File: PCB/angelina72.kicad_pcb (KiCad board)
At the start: 2 copper layers, 176.4 x 111.6 mm, 88 parts, among them J1 MJ-4PP-9, J2 LED, SW1 KEY_SWITCH, SW10 KEY_SWITCH, SW11 KEY_SWITCH, SW12 KEY_SWITCH, SW13 KEY_SWITCH, SW14 KEY_SWITCH, SW15 KEY_SWITCH, SW16 KEY_SWITCH, SW17 KEY_SWITCH, SW18 KEY_SWITCH, SW19 KEY_SWITCH, SW2 KEY_SWITCH, SW20 KEY_SWITCH, SW21 KEY_SWITCH, SW22 KEY_SWITCH, SW23 KEY_SWITCH, SW24 KEY_SWITCH, SW25 KEY_SWITCH, SW26 KEY_SWITCH, SW27 KEY_SWITCH, SW28 KEY_SWITCH, SW29 KEY_SWITCH, SW3 KEY_SWITCH, SW30 KEY_SWITCH, SW31 KEY_SWITCH, SW32 KEY_SWITCH, SW33 KEY_SWITCH, SW34 KEY_SWITCH, SW35 KEY_SWITCH, SW36 KEY_SWITCH, SW4 KEY_SWITCH, SW5 KEY_SWITCH, SW6 KEY_SWITCH, SW7 KEY_SWITCH, SW8 KEY_SWITCH, SW9 KEY_SWITCH, U1 ProMicro

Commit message: Update PCB, top plate
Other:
- outline, holes or cut-outs redrawn
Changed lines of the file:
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@@
   (gr_arc (start 65.649991 79.032478) (end 66.119003 78.949782) (angle -180) (layer Edge.Cuts) (width 0.05))
   (gr_arc (start 65.319197 77.156422) (end 64.850181 77.239123) (angle -180) (layer Edge.Cuts) (width 0.05))
-  (gr_line (start 74.6796 119.271451) (end 68.582435 120.346568) (layer Edge.Cuts) (width 0.05))
-  (gr_arc (start 68.665108 120.815566) (end 68.582435 120.346568) (angle -180.0026468) (layer Edge.Cuts) (width 0.05))
-  (gr_arc (start 66.789075 121.146382) (end 66.87175 121.615378) (angle -180.0026468) (layer Edge.Cuts) (width 0.05))
+  (gr_line (start 74.6796 119.271451) (end 68.934197 120.284543) (layer Edge.Cuts) (width 0.05))
+  (gr_arc (start 69.016871 120.753541) (end 68.934197 120.284543) (angle -180.0026468) (layer Edge.Cuts) (width 0.05))
+  (gr_arc (start 67.140837 121.084357) (end 67.223513 121.553353) (angle -180.0026468) (layer Edge.Cuts) (width 0.05))
   (gr_arc (start 188.469026 37.71159) (end 188.945278 37.71159) (angle -90) (layer Edge.Cuts) (width 0.05))
   (gr_arc (start 189.421526 45.80784) (end 188.945276 45.80784) (angle -90.00336866) (layer Edge.Cuts) (width 0.05))
@@
   (gr_line (start 188.945278 37.71159) (end 188.945276 45.80784) (layer Edge.Cuts) (width 0.05))
   (gr_line (start 110.18339 37.235327) (end 188.469026 37.23534) (layer Edge.Cuts) (width 0.05))
-  (gr_arc (start 70.014347 139.437938) (end 69.545332 139.52064) (angle -90) (layer Edge.Cuts) (width 0.05))
+  (gr_arc (start 70.36611 139.375912) (end 69.897094 139.458614) (angle -90) (layer Edge.Cuts) (width 0.05))
   (gr_arc (start 91.685142 39.501907) (end 91.623117 39.150143) (angle -90.00016041) (layer Edge.Cuts) (width 0.05))
   (gr_arc (start 90.981305 39.626012) (end 91.043696 39.978029) (angle -89.94903567) (layer Edge.Cuts) (width 0.05))
@@
   (gr_arc (start 39.111605 67.027821) (end 38.64259 67.110521) (angle -90) (layer Edge.Cuts) (width 0.05))
   (gr_arc (start 36.134407 50.143292) (end 36.051709 49.674278) (angle -90) (layer Edge.Cuts) (width 0.05))
-  (gr_arc (start 66.954449 122.084395) (end 66.871749 121.615379) (angle -90) (layer Edge.Cuts) (width 0.05))
+  (gr_arc (start 67.306212 122.02237) (end 67.223512 121.553354) (angle -90) (layer Edge.Cuts) (width 0.05))
   (gr_arc (start 57.71237 121.779635) (end 57.243356 121.862334) (angle -90) (layer Edge.Cuts) (width 0.05))
-  (gr_line (start 66.706377 120.677387) (end 57.795072 122.248649) (layer Edge.Cuts) (width 0.05))
+  (gr_line (start 67.05814 120.615365) (end 57.795072 122.248649) (layer Edge.Cuts) (width 0.05))
   (gr_arc (start 74.596899 118.802437) (end 74.6796 119.271451) (angle -90) (layer Edge.Cuts) (width 0.05))
   (gr_arc (start 75.700329 119.575067) (end 75.783028 120.044081) (angle -90) (layer Edge.Cuts) (width 0.05))
@@
   (gr_arc (start 62.189618 64.892932) (end 62.658632 64.810231) (angle -90) (layer Edge.Cuts) (width 0.05))
   (gr_arc (start 62.96225 63.789501) (end 63.431262 63.706802) (angle -90) (layer Edge.Cuts) (width 0.05))
-  (gr_line (start 75.783028 120.044081) (end 68.747804 121.28456) (layer Edge.Cuts) (width 0.05))
+  (gr_line (start 75.783028 120.044081) (end 69.099566 121.222535) (layer Edge.Cuts) (width 0.05))
   (gr_line (start 72.861344 100.731779) (end 75.218296 114.098697) (layer Edge.Cuts) (width 0.05))
   (gr_line (start 67.384976 101.213813) (end 72.309631 100.345462) (layer Edge.Cuts) (width 0.05))
@@
   (gr_line (start 56.61753 59.346881) (end 54.75678 48.794054) (layer Edge.Cuts) (width 0.05))
   (gr_line (start 53.81875 48.959451) (end 55.679498 59.512286) (layer Edge.Cuts) (width 0.05))
-  (gr_line (start 70.097047 139.906952) (end 117.542847 131.540747) (layer Edge.Cuts) (width 0.05))
-  (gr_line (start 66.485435 122.167095) (end 69.545332 139.52064) (layer Edge.Cuts) (width 0.05))
+  (gr_line (start 70.448812 139.844928) (end 117.542847 131.540747) (layer Edge.Cuts) (width 0.05))
+  (gr_line (start 66.837197 122.10507) (end 69.897094 139.458614) (layer Edge.Cuts) (width 0.05))
   (gr_line (start 54.100759 104.039777) (end 57.243356 121.862334) (layer Edge.Cuts) (width 0.05))
   (gr_line (start 48.624392 104.521811) (end 53.549043 103.653463) (layer Edge.Cuts) (width 0.05))
@@
   (segment (start 39.022628 57.467424) (end 37.94025 59.013216) (width 0.25) (layer B.Cu) (net 48))
   (segment (start 38.723626 55.771707) (end 39.022628 57.467424) (width 0.25) (layer B.Cu) (net 48))
-  (via (at 38.312406 61.12381) (size 0.8) (drill 0.4) (layers F.Cu B.Cu) (net 48) (status 1000000))
+  (via (at 38.312406 61.12381) (size 0.8) (drill 0.4) (layers F.Cu B.Cu) (net 48))
   (segment (start 44.463949 65.842279) (end 40.587526 66.525797) (width 0.25) (layer B.Cu) (net 48))
   (segment (start 39.078625 65.469253) (end 38.312406 61.12381) (width 0.25) (layer B.Cu) (net 48))

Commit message: Update PCB, top plate
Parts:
- removed the REF** at (126.8, 91.6)
- removed the REF** at (110.5, 92.4)
- removed the REF** at (77.9, 97.6)
- removed the REF** at (160.1, 91.6)
- moved U1 17.4 mm to (207.9, 80.6), turned to 350 degrees
- moved D34 17.1 mm to (197.3, 62.5), turned to 350 degrees
- moved RSW1 16.8 mm to (209.7, 111.6), turned to 80 degrees
- moved SW34 16.4 mm to (190.5, 58.9), turned to 350 degrees
- moved J1 16.4 mm to (206.8, 103.1), turned to 260 degrees
- moved REF** 16.3 mm to (205.9, 123.3), turned to 350 degrees
- moved D29 15.7 mm to (181.5, 54.6), turned to 350 degrees
- moved SW1 15.2 mm to (56.8, 46.3), turned to 0 degrees
- moved SW35 15.1 mm to (197.5, 134.0), turned to 320 degrees
- moved D30 14.7 mm to (188.3, 75.2), turned to 350 degrees
- moved REF** 14.6 mm to (196.0, 100.2), turned to 350 degrees
- moved SW29 14.3 mm to (171.7, 55.6), turned to 350 degrees
- moved REF** 14.2 mm to (179.5, 65.9), turned to 0 degrees
- moved SW36 14.0 mm to (185.3, 148.5), turned to 320 degrees
- moved D1 14.0 mm to (64.4, 49.4), turned to 0 degrees
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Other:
- board size 176.4 x 111.6 mm -> 172.2 x 124.6 mm

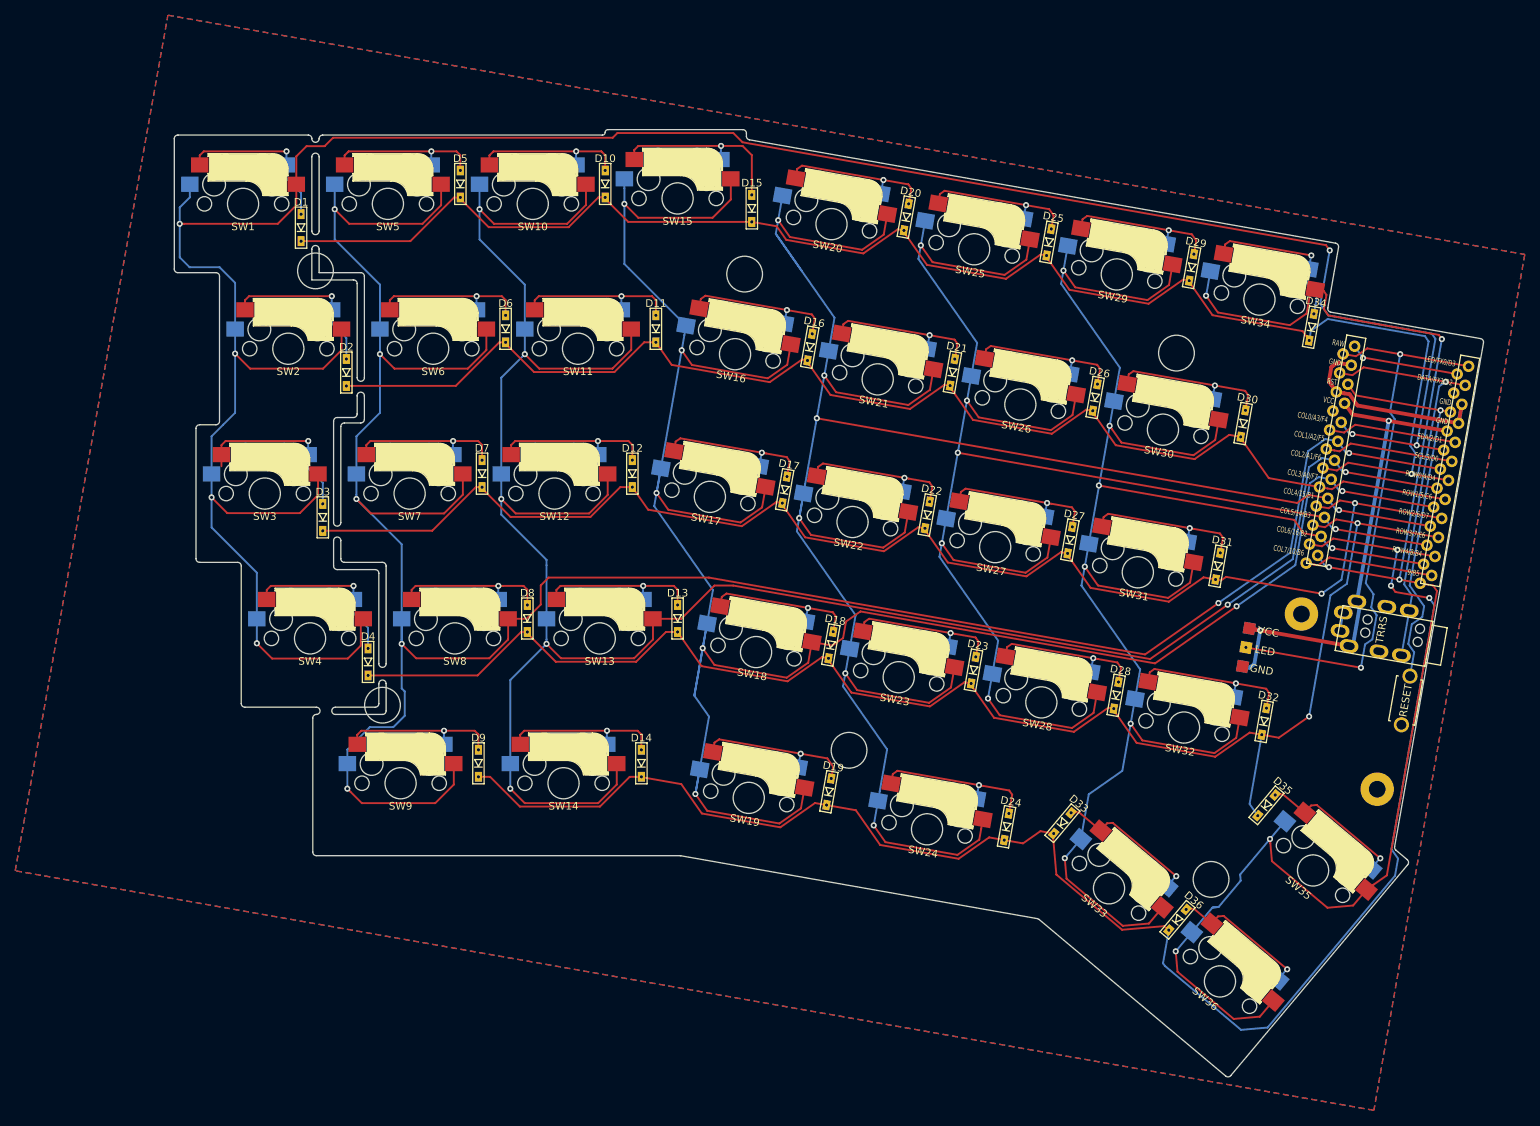
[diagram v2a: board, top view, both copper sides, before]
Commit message: Add bottom plate
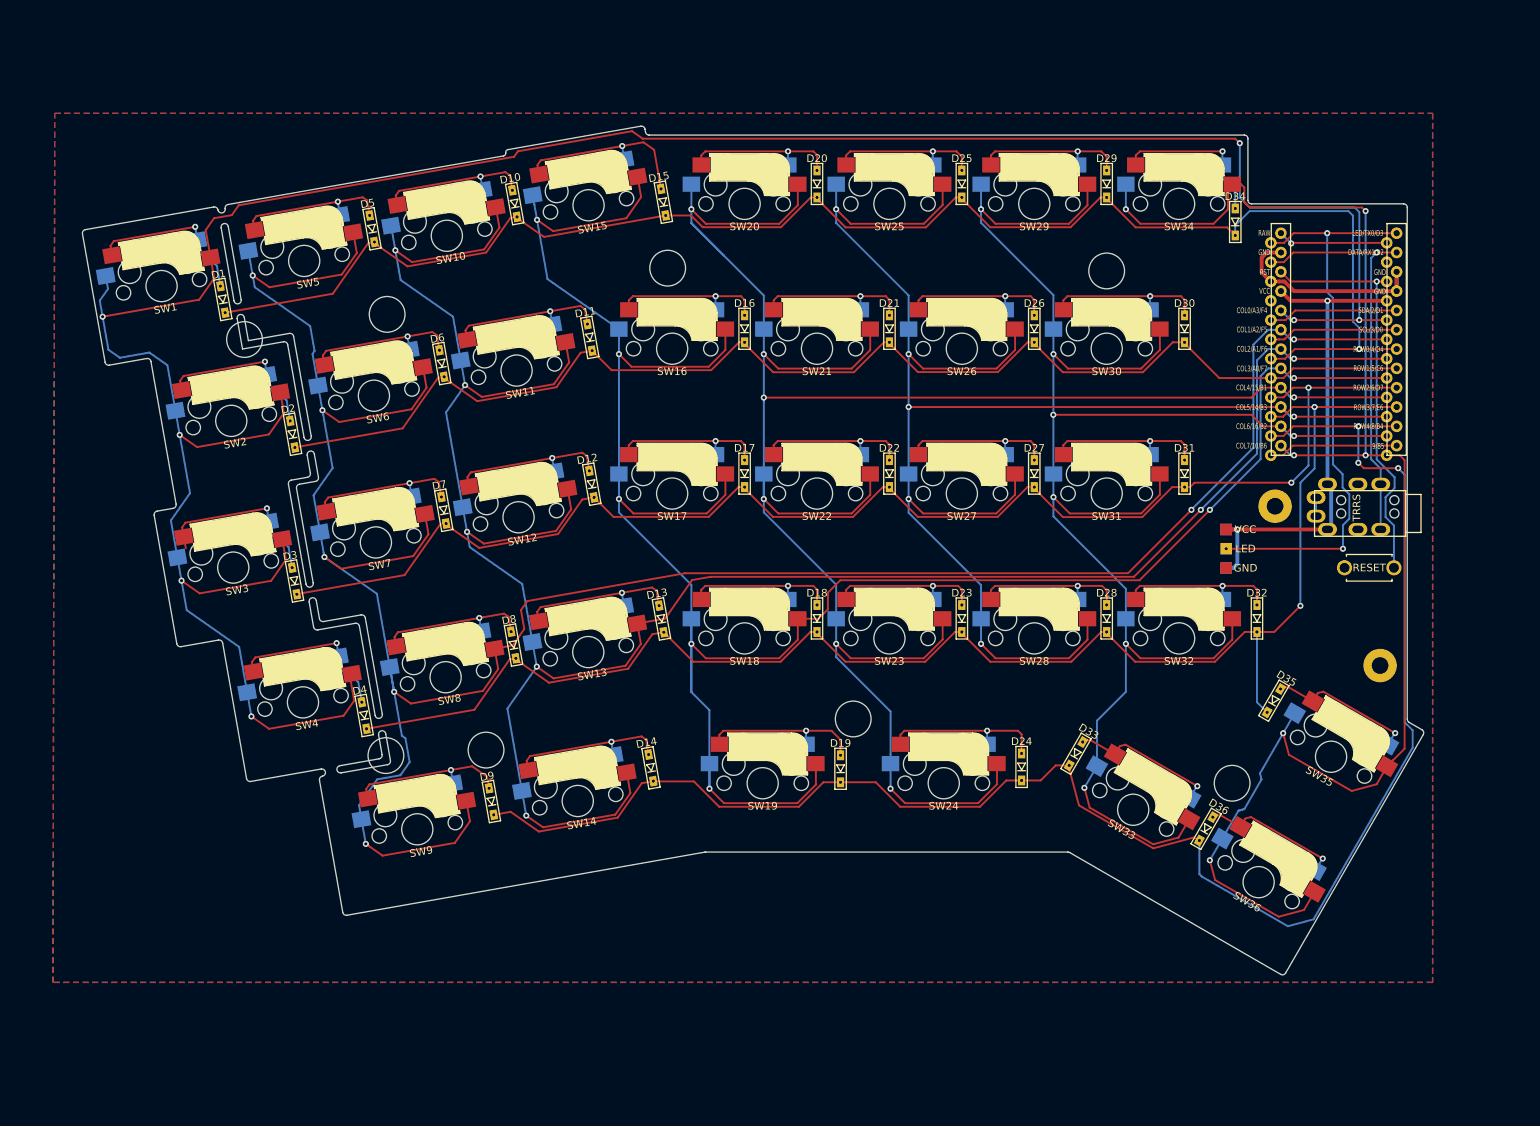
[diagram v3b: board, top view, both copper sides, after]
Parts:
- added REF**: Credit, angelina72:Credit, F.Cu at (137.0, 130.1)
- added REF**: M2_Spacer, angelina72:M2_Spacer, F.Cu at (88.7, 118.1)
- added REF**: M2_Spacer, angelina72:M2_Spacer, F.Cu at (75.7, 60.8)
- moved RSW1 18.1 mm to (204.9, 94.1), turned to 0 degrees
- moved U1 17.4 mm to (200.9, 64.6), turned to 0 degrees
- moved D34 17.1 mm to (187.3, 48.7), turned to 0 degrees
- moved SW34 16.4 mm to (179.9, 46.3), turned to 0 degrees
- moved J1 16.4 mm to (203.7, 87.0), turned to 270 degrees
- moved REF** 16.3 mm to (206.3, 107.0), turned to 0 degrees
- moved D29 15.7 mm to (170.4, 43.7), turned to 0 degrees
- moved SW1 15.2 mm to (46.1, 57.1), turned to 10 degrees
- moved SW35 15.1 mm to (199.9, 119.0), turned to 330 degrees
- moved D30 14.7 mm to (180.6, 62.7), turned to 0 degrees
- moved REF** 14.6 mm to (192.5, 86.1), turned to 0 degrees
- moved SW29 14.3 mm to (160.8, 46.3), turned to 0 degrees
- moved REF** 14.2 mm to (170.4, 55.1), turned to 10 degrees
- moved SW36 14.0 mm to (190.4, 135.5), turned to 330 degrees
- moved D1 14.0 mm to (54.1, 58.9), turned to 10 degrees
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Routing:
- net reset: track 51.4 -> 54.0 mm
- net row4: track 221.8 -> 220.9 mm
- net Net-(D19-Pad2): track 21.2 -> 21.7 mm
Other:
- board size 172.2 x 124.6 mm -> 176.4 x 111.6 mm

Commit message: Fix PCB, top plate, bottom plate
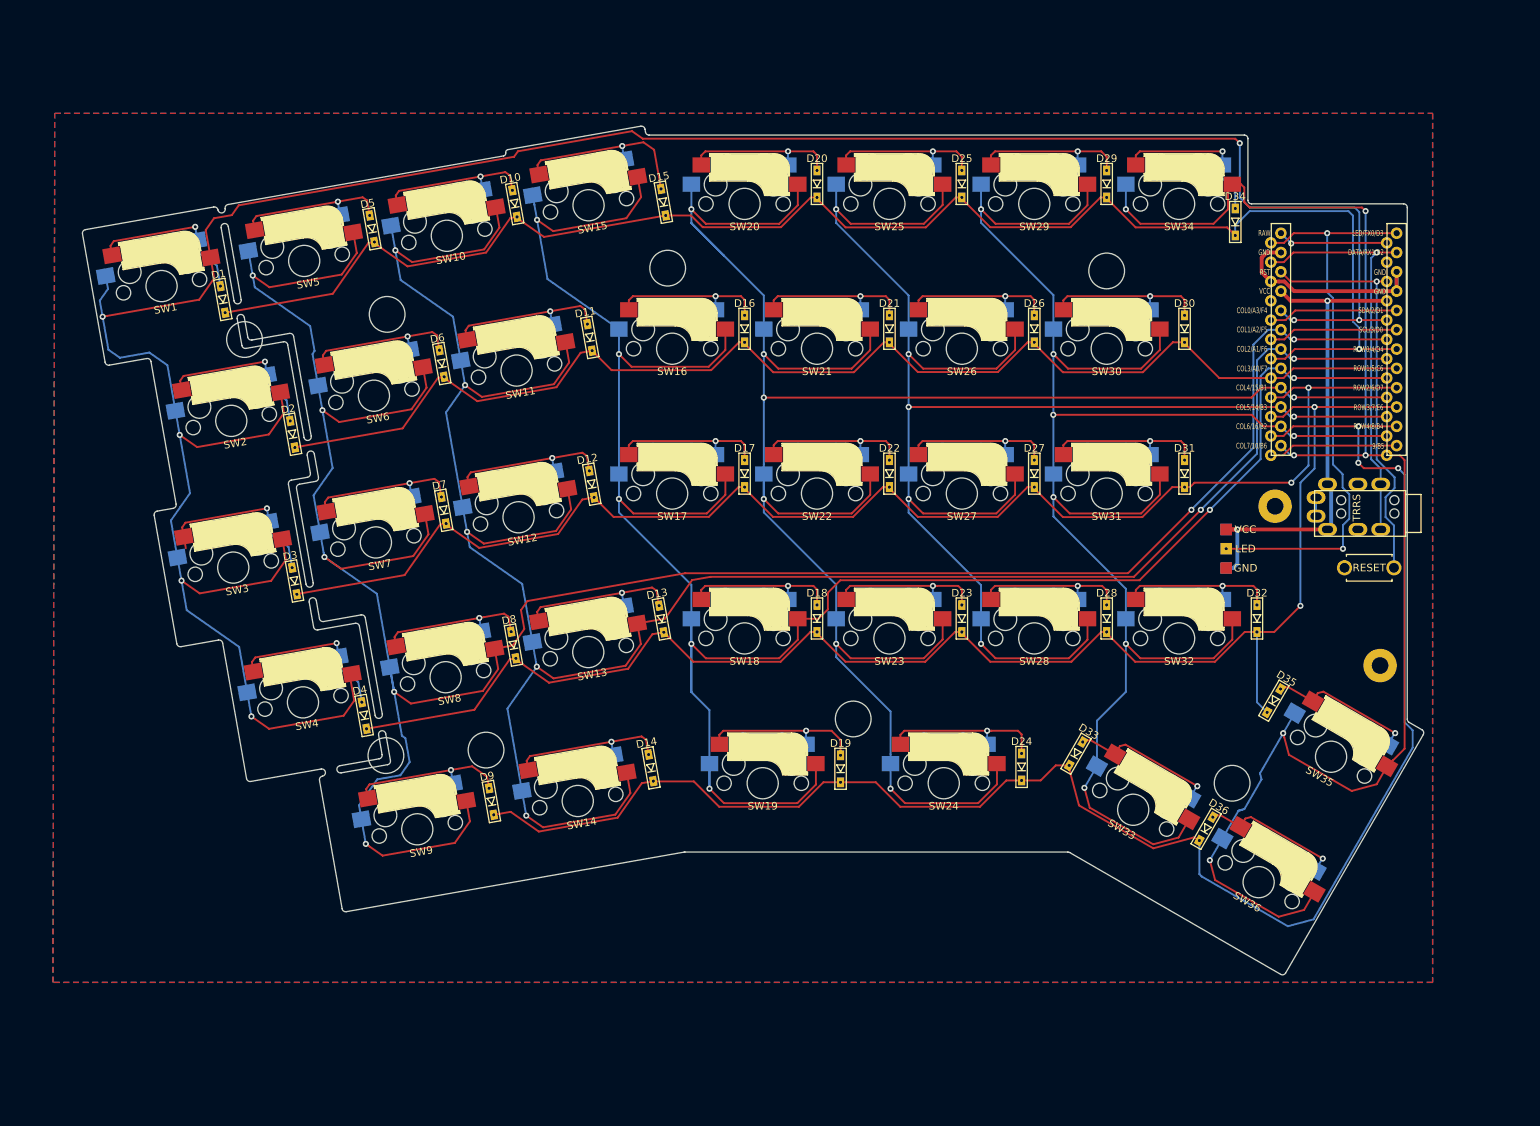
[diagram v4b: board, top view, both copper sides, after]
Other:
- outline, holes or cut-outs redrawn

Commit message: Update PCBs
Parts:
- added REF**: Layout_Outline_PromicroBase, angelina72:Layout_Outline_PromicroBase, F.Cu at (113.2, 113.0)
- added REF**: Layout_Outline, angelina72:Layout_Outline, F.Cu at (113.2, 113.0)
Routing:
- net col4: track 275.3 -> 269.2 mm
- net Net-(D3-Pad2): track 23.5 -> 22.0 mm
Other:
- outline, holes or cut-outs redrawn
